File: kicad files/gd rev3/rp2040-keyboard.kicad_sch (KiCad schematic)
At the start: 49 parts, among them J13 SWD, J14 USB_A, J21 KBD Serial, Q3 BC817, SW4 KBD RESET, SW5 KBD Boot Sel, U14 RP2040, U15 MIC5504-3.3YM5, U16 74HC245, U17 W25Q128JVS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

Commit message: 221 - added GND. lol.
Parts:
- D7: value 5V_PWR -> 5V_2040_PWR
- D9: value 3V3_PWR -> KBD_L
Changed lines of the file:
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@@
       (effects (font (size 1.27 1.27)) (justify right))
     )
-    (property "Value" "3V3_PWR" (id 1) (at 283.21 133.3499 90)
+    (property "Value" "KBD_L" (id 1) (at 283.21 133.3499 90)
       (effects (font (size 1.27 1.27)) (justify right))
     )
@@
       (effects (font (size 1.27 1.27)) (justify right))
     )
-    (property "Value" "5V_PWR" (id 1) (at 95.25 36.8299 90)
+    (property "Value" "5V_2040_PWR" (id 1) (at 95.25 36.8299 90)
       (effects (font (size 1.27 1.27)) (justify right))
     )

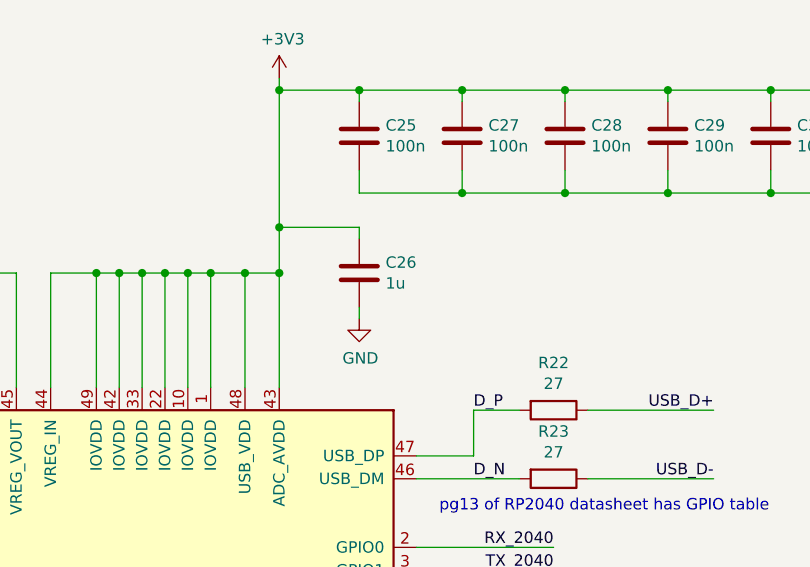
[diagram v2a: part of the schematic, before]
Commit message: 237: audio placement swapped, now drc check
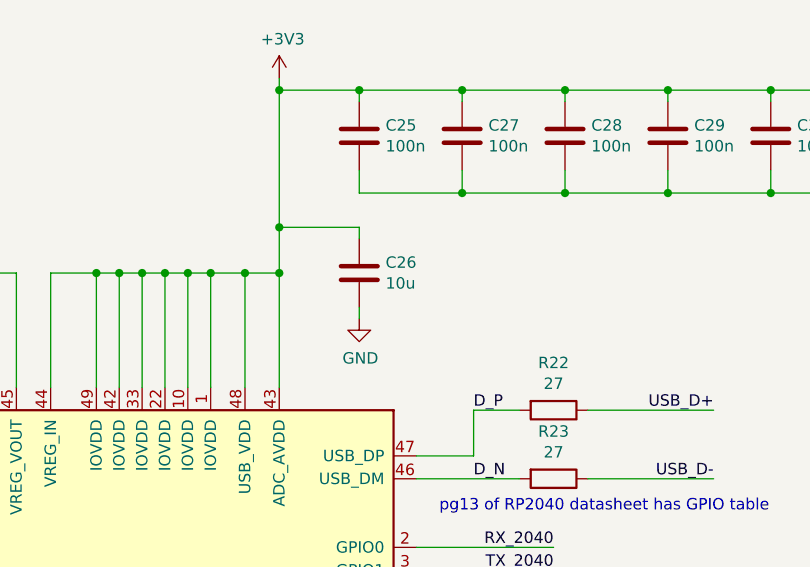
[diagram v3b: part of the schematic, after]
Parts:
- C26: value 1u -> 10u; footprint Capacitor_SMD:C_0603_1608Metric -> Capacitor_SMD:C_0805_2012Metric
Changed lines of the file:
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@@
       (effects (font (size 1.27 1.27)) (justify left))
     )
-    (property "Value" "1u" (id 1) (at 221.361 79.883 0)
+    (property "Value" "10u" (id 1) (at 221.361 79.883 0)
       (effects (font (size 1.27 1.27)) (justify left))
     )
-    (property "Footprint" "Capacitor_SMD:C_0603_1608Metric" (id 2) (at 219.4052 82.55 0)
+    (property "Footprint" "Capacitor_SMD:C_0805_2012Metric" (id 2) (at 219.4052 82.55 0)
       (effects (font (size 1.27 1.27)) hide)
     )

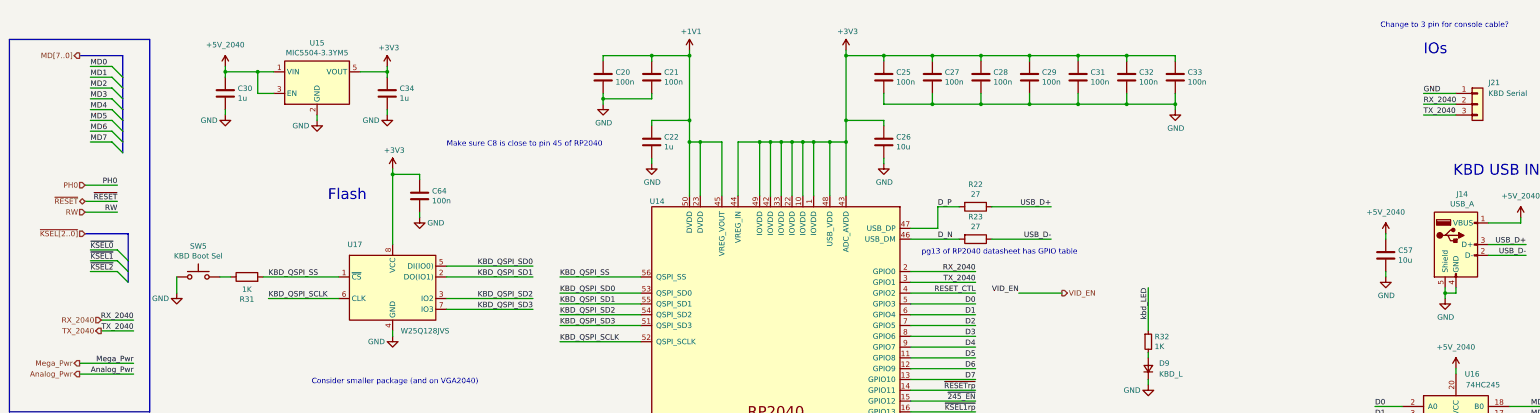
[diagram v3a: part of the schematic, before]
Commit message: 230: solder pads to swap RX/TX between KBD and VID
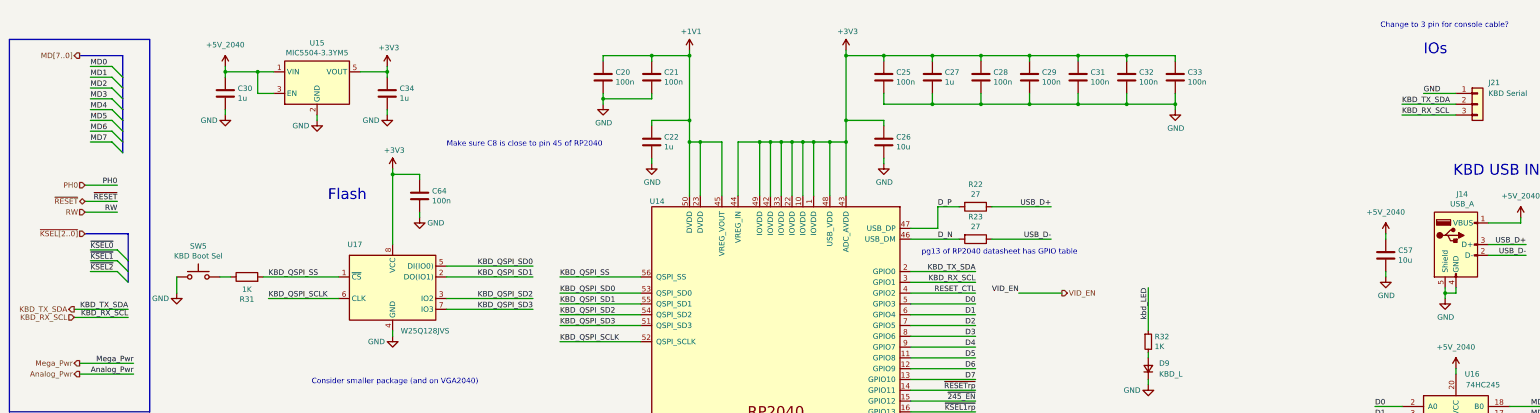
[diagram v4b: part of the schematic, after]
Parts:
- C27: value 100n -> 1u
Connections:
- net RX_2040 renamed KBD_TX_SDA
- net TX_2040 renamed KBD_RX_SCL
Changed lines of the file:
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@@
     (stroke (width 0) (type default) (color 0 0 0 0))
   )
-  (wire (pts (xy 41.91 123.19) (xy 34.29 123.19))
+  (wire (pts (xy 27.94 120.015) (xy 40.64 120.015))
     (stroke (width 0) (type default) (color 0 0 0 0))
   )
@@
     (stroke (width 0) (type default) (color 0 0 0 0))
   )
-  (wire (pts (xy 41.91 120.65) (xy 34.29 120.65))
+  (wire (pts (xy 27.94 118.11) (xy 40.64 118.11))
     (stroke (width 0) (type default) (color 0 0 0 0))
   )
@@
     (stroke (width 0) (type default) (color 0 0 0 0))
   )
-  (wire (pts (xy 345.44 69.85) (xy 353.06 69.85))
+  (wire (pts (xy 340.36 69.85) (xy 353.06 69.85))
     (stroke (width 0) (type default) (color 0 0 0 0))
   )
@@
     (stroke (width 0) (type default) (color 0 0 0 0))
   )
-  (wire (pts (xy 345.44 72.39) (xy 353.06 72.39))
+  (wire (pts (xy 340.36 72.39) (xy 353.06 72.39))
     (stroke (width 0) (type default) (color 0 0 0 0))
   )
@@
     (effects (font (size 1.27 1.27)) (justify right bottom))
   )
-  (label "RX_2040" (at 41.91 120.65 180)
-    (effects (font (size 1.27 1.27)) (justify right bottom))
-  )
   (label "MD4" (at 374.65 151.13 180)
     (effects (font (size 1.27 1.27)) (justify right bottom))
@@
     (effects (font (size 1.27 1.27)) (justify right bottom))
   )
-  (label "TX_2040" (at 240.03 111.76 180)
+  (label "KBD_RX_SCL" (at 240.03 111.76 180)
     (effects (font (size 1.27 1.27)) (justify right bottom))
   )
@@
     (effects (font (size 1.27 1.27)) (justify left bottom))
   )
+  (label "KBD_TX_SDA" (at 40.64 118.11 180)
+    (effects (font (size 1.27 1.27)) (justify right bottom))
+  )
   (label "MD0" (at 374.65 140.97 180)
     (effects (font (size 1.27 1.27)) (justify right bottom))
@@
     (effects (font (size 1.27 1.27)) (justify right bottom))
   )
+  (label "KBD_RX_SCL" (at 340.36 72.39 0)
+    (effects (font (size 1.27 1.27)) (justify left bottom))
+  )
   (label "SWD" (at 132.08 190.5 180)
     (effects (font (size 1.27 1.27)) (justify right bottom))
@@
     (effects (font (size 1.27 1.27)) (justify right bottom))
   )
-  (label "RX_2040" (at 240.03 109.22 180)
+  (label "KBD_TX_SDA" (at 240.03 109.22 180)
     (effects (font (size 1.27 1.27)) (justify right bottom))
   )
@@
     (effects (font (size 1.27 1.27)) (justify left bottom))
   )
+  (label "KBD_TX_SDA" (at 340.36 69.85 0)
+    (effects (font (size 1.27 1.27)) (justify left bottom))
+  )
   (label "MD1" (at 374.65 143.51 180)
     (effects (font (size 1.27 1.27)) (justify right bottom))
@@
     (effects (font (size 1.27 1.27)) (justify right bottom))
   )
+  (label "KBD_RX_SCL" (at 40.64 120.015 180)
+    (effects (font (size 1.27 1.27)) (justify right bottom))
+  )
   (label "RW" (at 133.35 228.6 0)
     (effects (font (size 1.27 1.27)) (justify left bottom))
@@
     (effects (font (size 1.27 1.27)) (justify left bottom))
   )
-  (label "RX_2040" (at 345.44 69.85 0)
-    (effects (font (size 1.27 1.27)) (justify left bottom))
-  )
   (label "~{KSEL0}" (at 31.75 104.14 0)
     (effects (font (size 1.27 1.27)) (justify left bottom))
@@
     (effects (font (size 1.27 1.27)) (justify left bottom))
   )
-  (label "TX_2040" (at 41.91 123.19 180)
-    (effects (font (size 1.27 1.27)) (justify right bottom))
-  )
   (label "SWCLK" (at 147.32 173.99 0)
     (effects (font (size 1.27 1.27)) (justify left bottom))
@@
     (effects (font (size 1.27 1.27)) (justify left bottom))
   )
-  (label "TX_2040" (at 345.44 72.39 0)
-    (effects (font (size 1.27 1.27)) (justify left bottom))
-  )
   (label "KBD_QSPI_SS" (at 142.24 110.49 0)
     (effects (font (size 1.27 1.27)) (justify left bottom))
@@
     (effects (font (size 1.27 1.27)) (justify right bottom))
   )
-  (hierarchical_label "TX_2040" (shape output) (at 34.29 123.19 180)
+  (hierarchical_label "KBD_RX_SCL" (shape input) (at 27.94 120.015 180)
     (effects (font (size 1.27 1.27)) (justify right))
   )
@@
     (effects (font (size 1.27 1.27)) (justify left))
   )
-  (hierarchical_label "RX_2040" (shape input) (at 34.29 120.65 180)
+  (hierarchical_label "KBD_TX_SDA" (shape output) (at 27.94 118.11 180)
     (effects (font (size 1.27 1.27)) (justify right))
   )
@@
       (effects (font (size 1.27 1.27)) (justify left))
     )
-    (property "Value" "100n" (id 1) (at 232.791 64.643 0)
-      (effects (font (size 1.27 1.27)) (justify left))
-    )
+    (property "Value" "1u" (id 1) (at 232.791 64.643 0)
+      (effects (font (size 1.27 1.27)) (justify left))
+    )

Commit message: 231: Fixed 5V_2040 reference value
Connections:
- net +5V: no longer C30.1, C57.1, C6.1, J14.1 (VBUS), R26.1, R53.2, U15.1 (VIN), U15.3 (EN), U16.20 (VCC)
- new net +5V_2040: C30.1, C57.1, C6.1, J14.1 (VBUS), R26.1, R53.2, U15.1 (VIN), U15.3 (EN), U16.20 (VCC)
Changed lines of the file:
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@@
     (pin "1")
   )
-  (symbol (lib_id "My Library:+5V_2040") (at 63.5 60.96 0) (unit 1)
+  (symbol (lib_name "+5V_2040_3") (lib_id "My Library:+5V_2040") (at 63.5 60.96 0) (unit 1)
     (in_bom yes) (on_board yes) (fields_autoplaced)
     (property "Reference" "#PWR0241" (id 0) (at 63.5 64.77 0)
@@
     (pin "2")
   )
-  (symbol (lib_id "My Library:+5V_2040") (at 336.55 100.33 0) (unit 1)
+  (symbol (lib_name "+5V_2040_6") (lib_id "My Library:+5V_2040") (at 336.55 100.33 0) (unit 1)
     (in_bom yes) (on_board yes) (fields_autoplaced)
     (property "Reference" "#PWR0251" (id 0) (at 336.55 104.14 0)
@@
     (pin "1")
   )
-  (symbol (lib_id "My Library:+5V_2040") (at 368.3 96.52 0) (unit 1)
+  (symbol (lib_name "+5V_2040_5") (lib_id "My Library:+5V_2040") (at 368.3 96.52 0) (unit 1)
     (in_bom yes) (on_board yes) (fields_autoplaced)
     (property "Reference" "#PWR0249" (id 0) (at 368.3 100.33 0)
@@
     (pin "2")
   )
-  (symbol (lib_id "My Library:+5V_2040") (at 353.06 132.08 0) (unit 1)
+  (symbol (lib_name "+5V_2040_1") (lib_id "My Library:+5V_2040") (at 353.06 132.08 0) (unit 1)
     (in_bom yes) (on_board yes) (fields_autoplaced)
     (property "Reference" "#PWR0256" (id 0) (at 353.06 135.89 0)
@@
     (pin "1")
   )
-  (symbol (lib_id "My Library:+5V_2040") (at 92.71 25.4 0) (unit 1)
+  (symbol (lib_name "+5V_2040_4") (lib_id "My Library:+5V_2040") (at 92.71 25.4 0) (unit 1)
     (in_bom yes) (on_board yes) (fields_autoplaced)
     (property "Reference" "#PWR0240" (id 0) (at 92.71 29.21 0)
@@
     (pin "1")
   )
-  (symbol (lib_id "My Library:+5V_2040") (at 298.45 224.79 0) (unit 1)
+  (symbol (lib_name "+5V_2040_2") (lib_id "My Library:+5V_2040") (at 298.45 224.79 0) (unit 1)
     (in_bom yes) (on_board yes) (fields_autoplaced)
     (property "Reference" "#PWR0229" (id 0) (at 298.45 228.6 0)

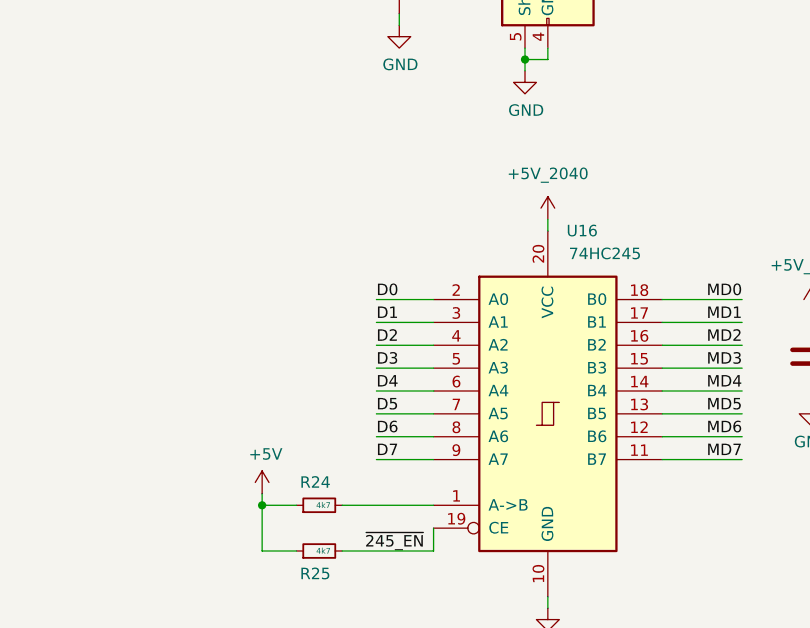
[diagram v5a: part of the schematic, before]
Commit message: 95: 5V (mega logic) routed/wired.
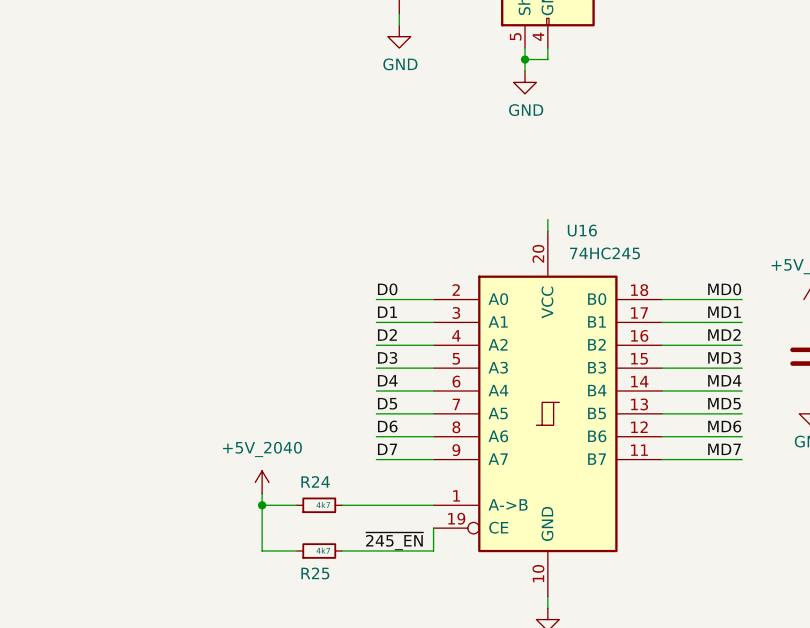
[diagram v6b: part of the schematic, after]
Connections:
- net +5V is gone; now on net +5V_2040: R24.1, R25.1
- net +5V_2040: no longer U16.20 (VCC)
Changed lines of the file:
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@@
-    (pin "1")
-  )
-  (symbol (lib_id "power:+5V") (at 321.31 162.56 0) (unit 1)
-    (in_bom yes) (on_board yes)
-    (property "Reference" "#PWR0244" (id 0) (at 321.31 166.37 0)
-      (effects (font (size 1.27 1.27)) hide)
-    )
-    (property "Value" "+5V" (id 1) (at 321.691 158.1658 0))
-    (property "Footprint" "" (id 2) (at 321.31 162.56 0)
-      (effects (font (size 1.27 1.27)) hide)
-    )
-    (property "Datasheet" "" (id 3) (at 321.31 162.56 0)
-      (effects (font (size 1.27 1.27)) hide)
-    )
     (pin "1")
   )
@@
     (pin "2")
   )
-  (symbol (lib_name "+5V_2040_1") (lib_id "My Library:+5V_2040") (at 353.06 132.08 0) (unit 1)
+  (symbol (lib_name "+5V_2040_1") (lib_id "My Library:+5V_2040") (at 321.31 162.56 0) (unit 1)
     (in_bom yes) (on_board yes) (fields_autoplaced)
-    (property "Reference" "#PWR0256" (id 0) (at 353.06 135.89 0)
-      (effects (font (size 1.27 1.27)) hide)
-    )
-    (property "Value" "+5V_2040" (id 1) (at 353.06 127 0))
-    (property "Footprint" "" (id 2) (at 353.06 132.08 0)
-      (effects (font (size 1.27 1.27)) hide)
-    )
-    (property "Datasheet" "" (id 3) (at 353.06 132.08 0)
-      (effects (font (size 1.27 1.27)) hide)
-    )
+    (property "Reference" "#PWR0256" (id 0) (at 321.31 166.37 0)
+      (effects (font (size 1.27 1.27)) hide)
+    )
+    (property "Value" "+5V_2040" (id 1) (at 321.31 157.48 0))
+    (property "Footprint" "" (id 2) (at 321.31 162.56 0)
+      (effects (font (size 1.27 1.27)) hide)
+    )
+    (property "Datasheet" "" (id 3) (at 321.31 162.56 0)
+      (effects (font (size 1.27 1.27)) hide)
+    )

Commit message: 33: seems like 3v3 is done now ...
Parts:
- C64: value 100n -> 1u; footprint Capacitor_SMD:C_0805_2012Metric -> Capacitor_SMD:C_0603_1608Metric
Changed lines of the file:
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@@
       (effects (font (size 1.27 1.27)) (justify left))
     )
-    (property "Value" "100n" (id 1) (at 112.141 92.583 0)
+    (property "Value" "1u" (id 1) (at 112.141 92.583 0)
       (effects (font (size 1.27 1.27)) (justify left))
     )
-    (property "Footprint" "Capacitor_SMD:C_0805_2012Metric" (id 2) (at 110.1852 95.25 0)
+    (property "Footprint" "Capacitor_SMD:C_0603_1608Metric" (id 2) (at 110.1852 95.25 0)
       (effects (font (size 1.27 1.27)) hide)
     )

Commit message: 15: time for a break
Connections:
- net +5V_2040: now also U16.20 (VCC)
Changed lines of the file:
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@@
     (pin "9")
+  )
+  (symbol (lib_name "+5V_2040_1") (lib_id "My Library:+5V_2040") (at 353.06 132.08 0) (unit 1)
+    (in_bom yes) (on_board yes) (fields_autoplaced)
+    (property "Reference" "#PWR?" (id 0) (at 353.06 135.89 0)
+      (effects (font (size 1.27 1.27)) hide)
+    )
+    (property "Value" "+5V_2040" (id 1) (at 353.06 127 0))
+    (property "Footprint" "" (id 2) (at 353.06 132.08 0)
+      (effects (font (size 1.27 1.27)) hide)
+    )
+    (property "Datasheet" "" (id 3) (at 353.06 132.08 0)
+      (effects (font (size 1.27 1.27)) hide)
+    )
+    (pin "1")
   )
   (symbol (lib_id "Device:C") (at 163.83 63.5 0) (unit 1)
